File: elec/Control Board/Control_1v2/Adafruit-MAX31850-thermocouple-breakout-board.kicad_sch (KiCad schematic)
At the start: 48 parts, among them J11 Con_01x02_2.5mm, J2 MAX31850K

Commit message: Add a 3D model for the JHT connector B2B-XH-A-GU.
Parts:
- J11: footprint Connector_JST:JST_XH_B2B-XH-AM_1x02_P2.50mm_Vertical -> PubInv_KiCad_PCB:JST_XH_B2B-XH-AM_1x02_P2.50mm_Vertical
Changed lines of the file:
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@@
       (effects (font (size 1.27 1.27)) (justify left))
     )
-    (property "Footprint" "Connector_JST:JST_XH_B2B-XH-AM_1x02_P2.50mm_Vertical" (at 317.5 171.45 0)
+    (property "Footprint" "PubInv_KiCad_PCB:JST_XH_B2B-XH-AM_1x02_P2.50mm_Vertical" (at 317.5 171.45 0)
       (effects (font (size 1.27 1.27)) hide)
     )
@@
       (effects (font (size 1.27 1.27)) (justify left))
     )
-    (property "Footprint" "Connector_JST:JST_XH_B2B-XH-AM_1x02_P2.50mm_Vertical" (at 191.77 223.52 0)
+    (property "Footprint" "PubInv_KiCad_PCB:JST_XH_B2B-XH-AM_1x02_P2.50mm_Vertical" (at 191.77 223.52 0)
       (effects (font (size 1.27 1.27)) hide)
     )
@@
       (effects (font (size 1.27 1.27)) (justify left))
     )
-    (property "Footprint" "Connector_JST:JST_XH_B2B-XH-AM_1x02_P2.50mm_Vertical" (at 181.61 156.21 0)
+    (property "Footprint" "PubInv_KiCad_PCB:JST_XH_B2B-XH-AM_1x02_P2.50mm_Vertical" (at 181.61 156.21 0)
       (effects (font (size 1.27 1.27)) hide)
     )
@@
       (effects (font (size 1.27 1.27)) (justify left))
     )
-    (property "Footprint" "Connector_JST:JST_XH_B2B-XH-AM_1x02_P2.50mm_Vertical" (at 411.48 128.27 0)
-      (effects (font (size 1.27 1.27)) hide)
-    )
+    (property "Footprint" "PubInv_KiCad_PCB:JST_XH_B2B-XH-AM_1x02_P2.50mm_Vertical" (at 411.48 128.27 0)
+      (effects (font (size 1.27 1.27)) hide)
+    )

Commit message: PCB V1.2. Add test points of many colors.
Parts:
- TP103: Cost NA -> 0.0696; Distributor 1 (none) -> JLCPCB; Distributor 1 PN (none) -> C5277086; MPN (none) -> RH-5000; Manufacturer (none) -> ronghe
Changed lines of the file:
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@@
       (effects (font (size 1.27 1.27)) hide)
     )
-    (property "Cost" "NA" (at 106.68 67.31 0)
+    (property "Cost" "0.0696" (at 106.68 67.31 0)
+      (effects (font (size 1.27 1.27)) hide)
+    )
+    (property "Description" "Test Points/Test Rings ROHS red" (at 106.68 67.31 0)
+      (effects (font (size 1.27 1.27)) hide)
+    )
+    (property "Distributor 1 PN" "C5277086" (at 106.68 67.31 0)
+      (effects (font (size 1.27 1.27)) hide)
+    )
+    (property "Distributor 1" "JLCPCB" (at 106.68 67.31 0)
+      (effects (font (size 1.27 1.27)) hide)
+    )
+    (property "MPN" "RH-5000 " (at 106.68 67.31 0)
+      (effects (font (size 1.27 1.27)) hide)
+    )
+    (property "Manufacturer" "ronghe " (at 106.68 67.31 0)
       (effects (font (size 1.27 1.27)) hide)
     )
@@
       (effects (font (size 1.27 1.27)) hide)
     )
-    (property "Cost" "NA" (at 175.26 214.63 0)
+    (property "Cost" "0.0696" (at 175.26 214.63 0)
+      (effects (font (size 1.27 1.27)) hide)
+    )
+    (property "Description" "Test Points/Test Rings ROHS red" (at 175.26 214.63 0)
+      (effects (font (size 1.27 1.27)) hide)
+    )
+    (property "Distributor 1 PN" "C5277086" (at 175.26 214.63 0)
+      (effects (font (size 1.27 1.27)) hide)
+    )
+    (property "Distributor 1" "JLCPCB" (at 175.26 214.63 0)
+      (effects (font (size 1.27 1.27)) hide)
+    )
+    (property "MPN" "RH-5000 " (at 175.26 214.63 0)
+      (effects (font (size 1.27 1.27)) hide)
+    )
+    (property "Manufacturer" "ronghe " (at 175.26 214.63 0)
       (effects (font (size 1.27 1.27)) hide)
     )
@@
       (effects (font (size 1.27 1.27)) hide)
     )
-    (property "Cost" "NA" (at 290.83 161.29 0)
+    (property "Cost" "0.0696" (at 290.83 161.29 0)
+      (effects (font (size 1.27 1.27)) hide)
+    )
+    (property "Description" "Test Points/Test Rings ROHS red" (at 290.83 161.29 0)
+      (effects (font (size 1.27 1.27)) hide)
+    )
+    (property "Distributor 1 PN" "C5277086" (at 290.83 161.29 0)
+      (effects (font (size 1.27 1.27)) hide)
+    )
+    (property "Distributor 1" "JLCPCB" (at 290.83 161.29 0)
+      (effects (font (size 1.27 1.27)) hide)
+    )
+    (property "MPN" "RH-5000 " (at 290.83 161.29 0)
+      (effects (font (size 1.27 1.27)) hide)
+    )
+    (property "Manufacturer" "ronghe " (at 290.83 161.29 0)
       (effects (font (size 1.27 1.27)) hide)
     )
@@
       (effects (font (size 1.27 1.27)) hide)
     )
-    (property "Cost" "NA" (at 384.81 118.11 0)
+    (property "Cost" "0.0696" (at 384.81 118.11 0)
+      (effects (font (size 1.27 1.27)) hide)
+    )
+    (property "Description" "Test Points/Test Rings ROHS red" (at 384.81 118.11 0)
+      (effects (font (size 1.27 1.27)) hide)
+    )
+    (property "Distributor 1" "JLCPCB" (at 384.81 118.11 0)
+      (effects (font (size 1.27 1.27)) hide)
+    )
+    (property "Distributor 1 PN" "C5277086" (at 384.81 118.11 0)
+      (effects (font (size 1.27 1.27)) hide)
+    )
+    (property "MPN" "RH-5000 " (at 384.81 118.11 0)
+      (effects (font (size 1.27 1.27)) hide)
+    )
+    (property "Manufacturer" "ronghe " (at 384.81 118.11 0)
       (effects (font (size 1.27 1.27)) hide)
     )
@@
       (effects (font (size 1.27 1.27)) hide)
     )
-    (property "Cost" "NA" (at 148.59 128.27 0)
-      (effects (font (size 1.27 1.27)) hide)
-    )
+    (property "Cost" "0.0696" (at 148.59 128.27 0)
+      (effects (font (size 1.27 1.27)) hide)
+    )
+    (property "Description" "Test Points/Test Rings ROHS red" (at 148.59 128.27 0)
+      (effects (font (size 1.27 1.27)) hide)
+    )
+    (property "Distributor 1 PN" "C5277086" (at 148.59 128.27 0)
+      (effects (font (size 1.27 1.27)) hide)
+    )
+    (property "Distributor 1" "JLCPCB" (at 148.59 128.27 0)
+      (effects (font (size 1.27 1.27)) hide)
+    )
+    (property "MPN" "RH-5000 " (at 148.59 128.27 0)
+      (effects (font (size 1.27 1.27)) hide)
+    )
+    (property "Manufacturer" "ronghe " (at 148.59 128.27 0)
+      (effects (font (size 1.27 1.27)) hide)
+    )

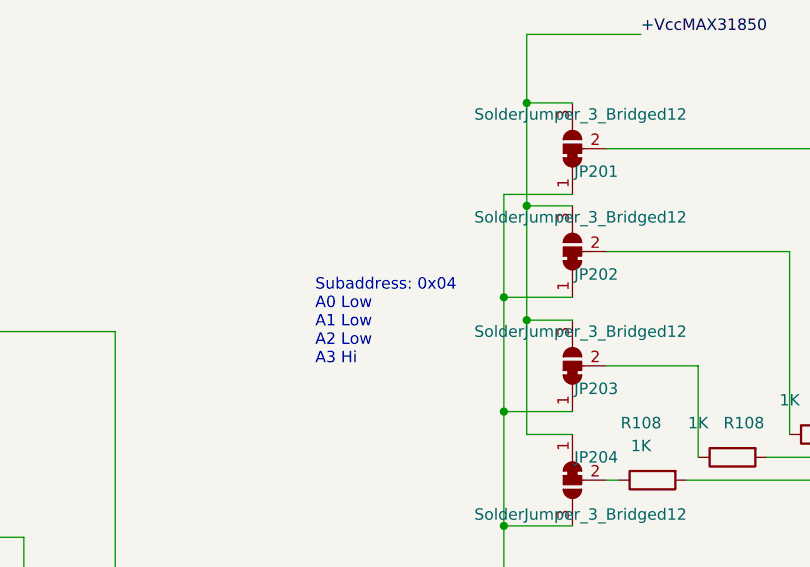
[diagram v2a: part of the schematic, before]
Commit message: Correct notes to schematic identifying subaddress on MAX31850.
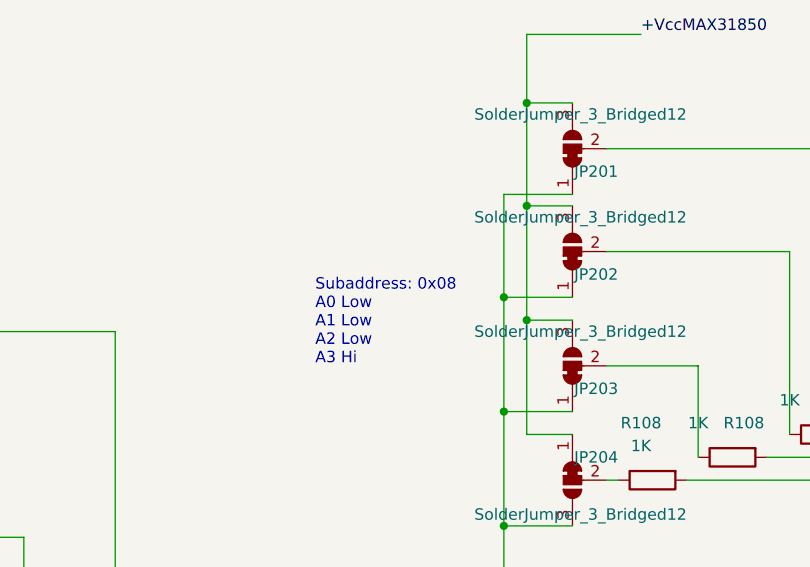
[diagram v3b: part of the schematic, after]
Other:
- note added: "Subaddress: 0x08 A0 Low A1 Low A2 Low A3 Hi"
- note removed: "Subaddress: 0x04 A0 Low A1 Low A2 Low A3 Hi"
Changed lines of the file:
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@@
     (effects (font (size 1.27 1.27)) (justify left bottom))
   )
-  (text "Subaddress: 0x04\nA0 Low\nA1 Low\nA2 Low\nA3 Hi\n" (at 309.245 95.25 0)
+  (text "Subaddress: 0x08\nA0 Low\nA1 Low\nA2 Low\nA3 Hi\n" (at 309.245 95.25 0)
     (effects (font (size 1.27 1.27)) (justify left bottom))
   )
